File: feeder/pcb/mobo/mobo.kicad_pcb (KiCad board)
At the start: 2 copper layers, 160.6 x 110 mm, 45 parts, among them J1 SPRING_FINGER_INTERFACE, J3 SWD_10, M1 DRIVE_MOTOR, M2 PEEL_MOTOR, SW1 BUTTON_1, SW2 BUTTON_2, SW3 RESET_BUTTON, SW4 TAPE_DETECT, SW5 FILM_TENSION, U1 STM32F030K6Tx, U2 VCNT2020, U3 MAX3485, U4 DRV8833PW, U5 AP1117-33, Y1 Crystal_GND24_Small

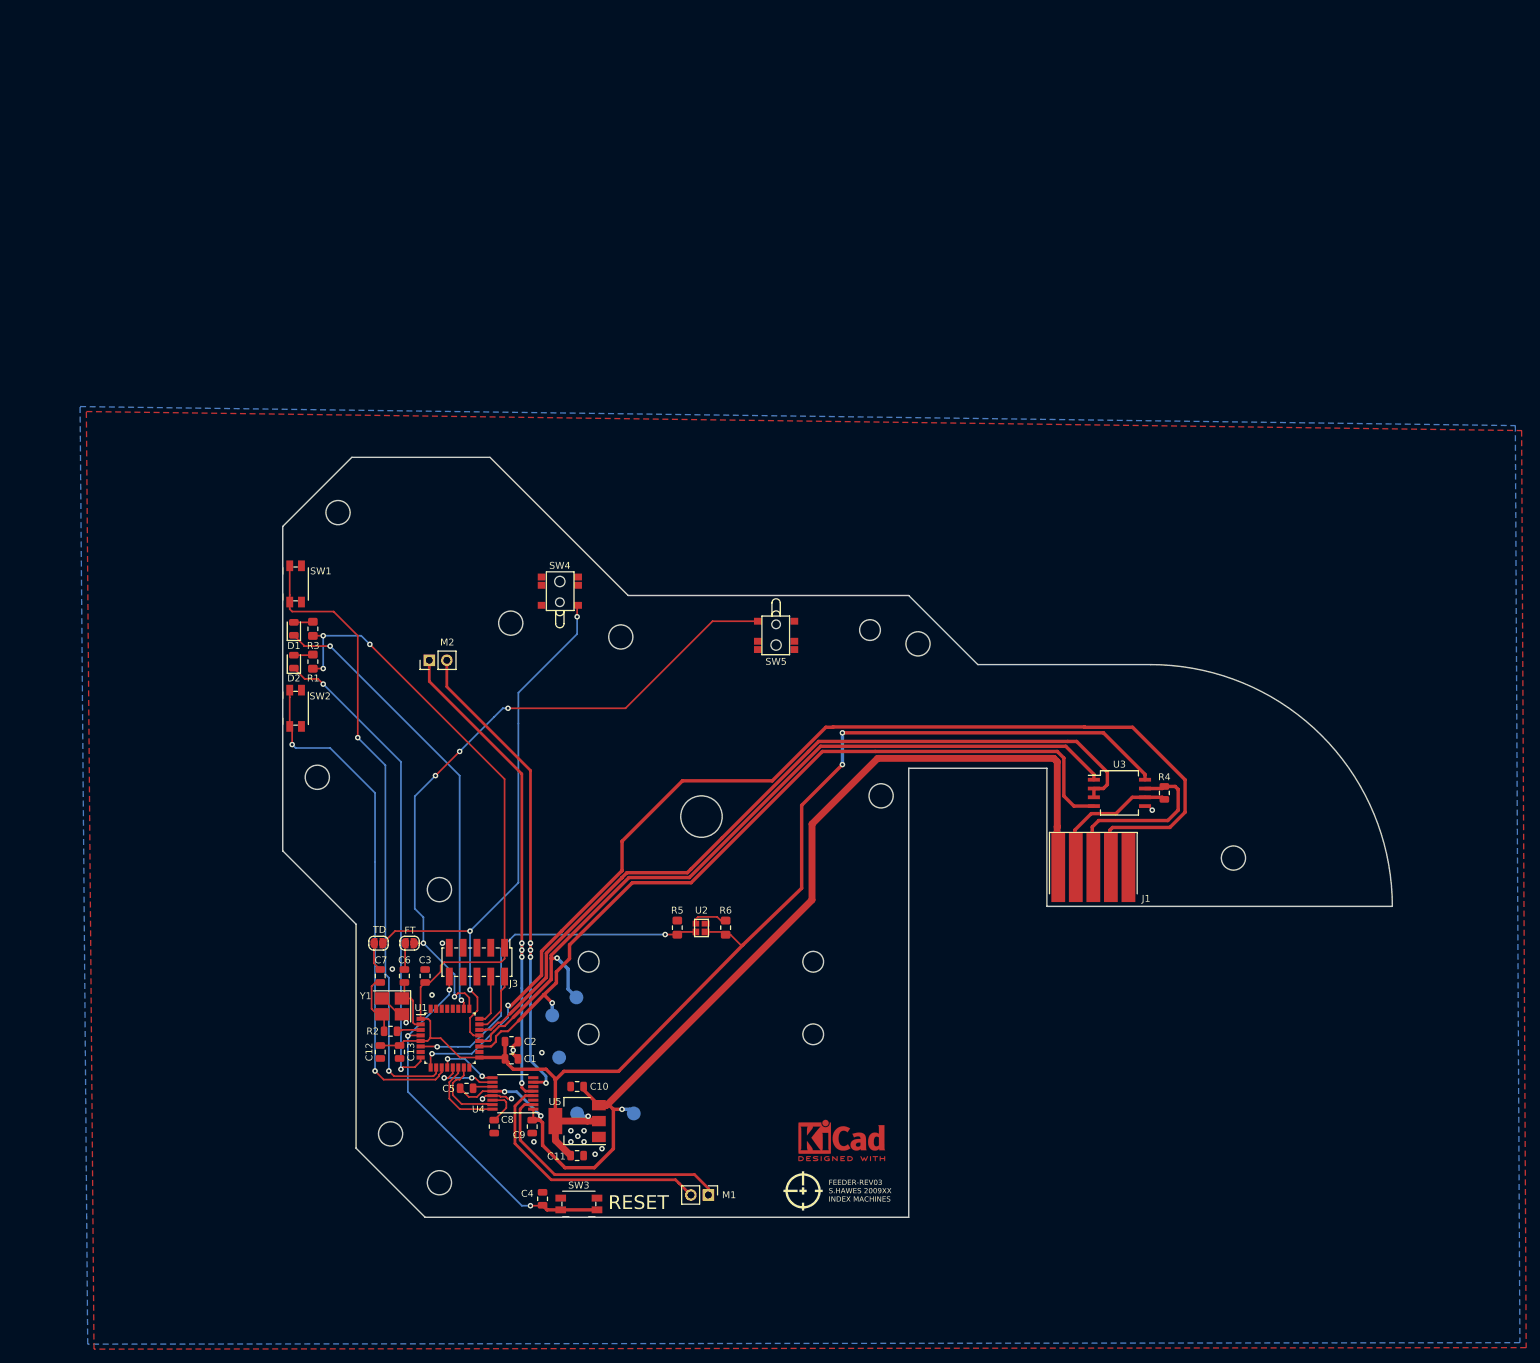
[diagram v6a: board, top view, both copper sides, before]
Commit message: this commit reflects boards ordered for rev04 of the feeder motherboard, rev02 of the indexing wheel, and rev02 of the feeder floor
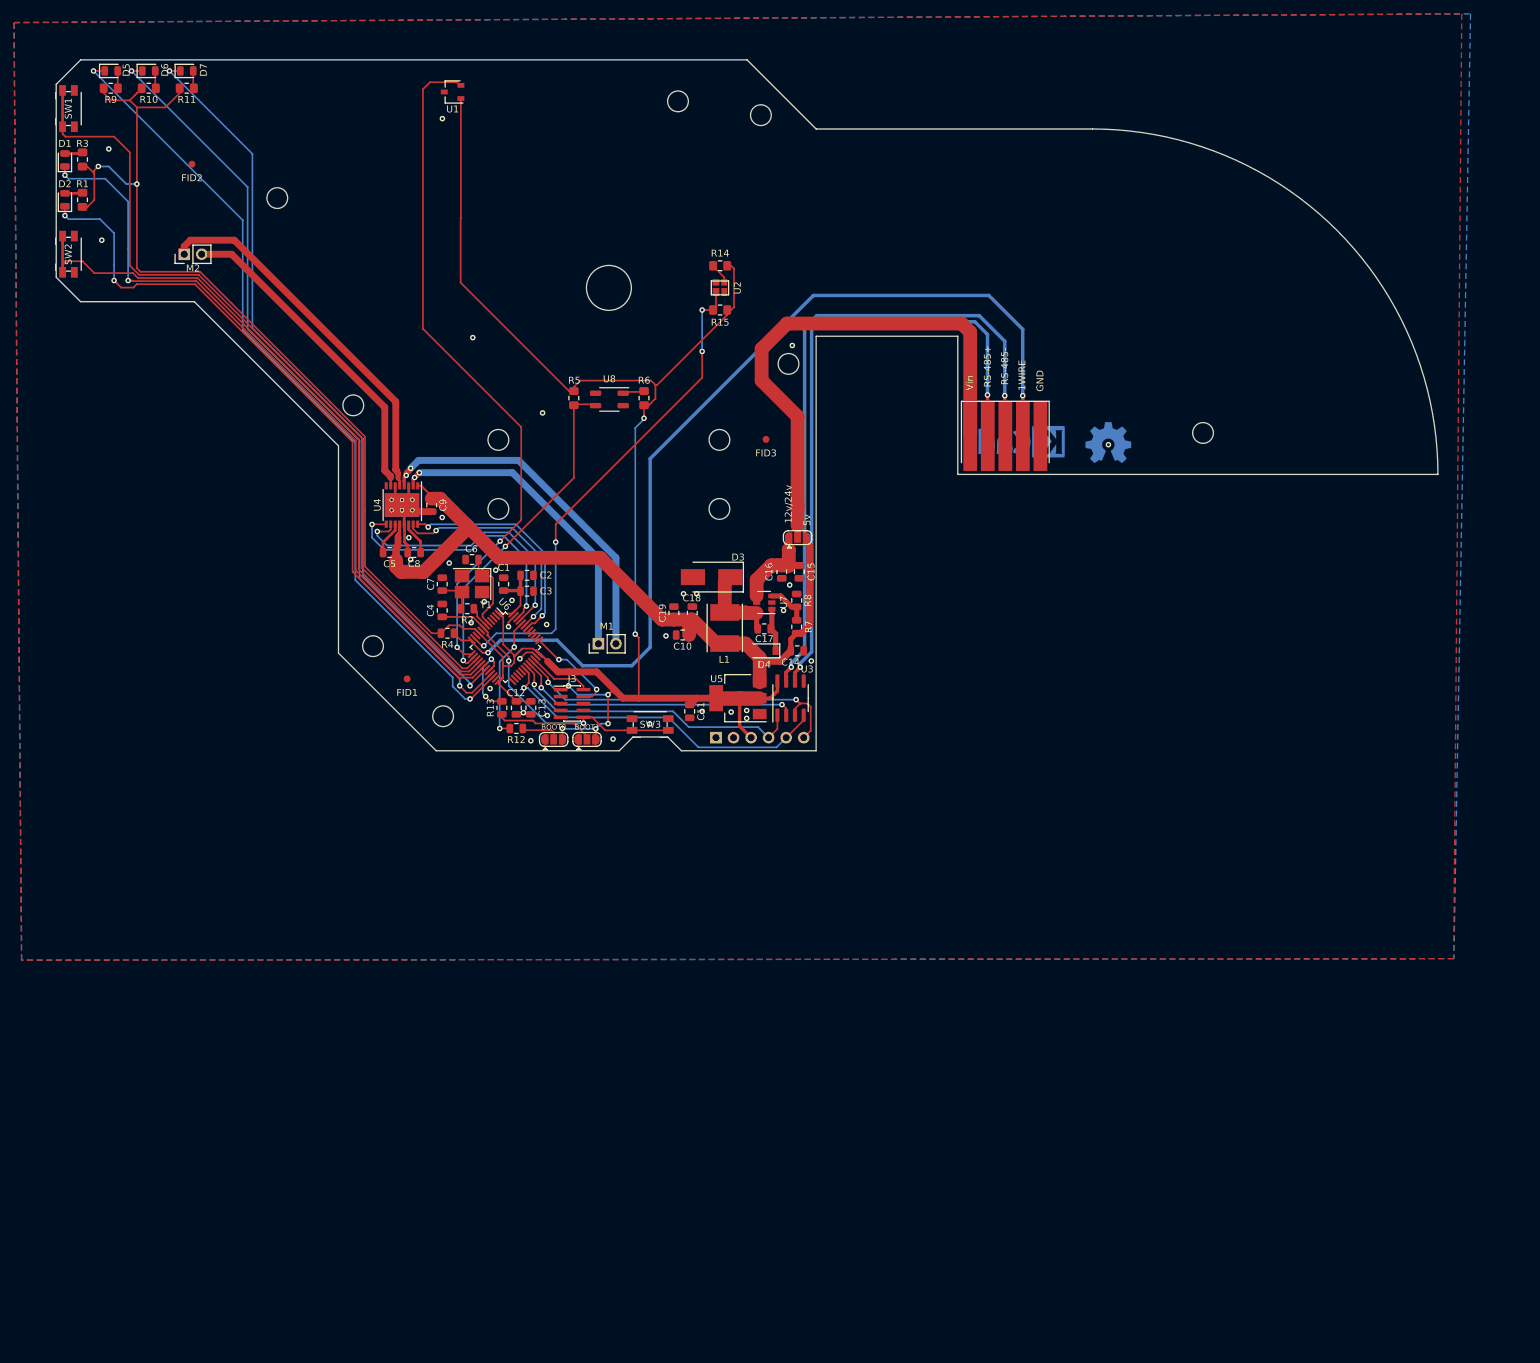
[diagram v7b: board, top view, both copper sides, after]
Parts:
- removed the REF** at (119.8, 161.8)
- removed SW4: TAPE_DETECT, index:K5-1624SA-01
- removed SW5: FILM_TENSION, index:K5-1624SA-01
- removed TP1: MCU_TX, TestPoint:TestPoint_Pad_D2.0mm
- removed TP2, TP3, TP4, TP5: MCU_RX, TestPoint:TestPoint_Pad_D2.0mm
- added C14: 100uF, Capacitor_SMD:C_0805_2012Metric, F.Cu at (113.4, 90.9)
- added C15: 4.7uF, Capacitor_SMD:C_0805_2012Metric, F.Cu at (113.7, 79.5)
- added C16: 4.7uF, Capacitor_SMD:C_0805_2012Metric, F.Cu at (111.1, 79.5)
- added C17: 0.1uF, Capacitor_SMD:C_0805_2012Metric, F.Cu at (108.6, 87.8)
- added C18: 10uF, Capacitor_SMD:C_0805_2012Metric, F.Cu at (98.2, 85.5)
- added C19: 10uF, Capacitor_SMD:C_0805_2012Metric, F.Cu at (95.5, 85.5)
- added D3: B140, Diode_SMD:D_SMB_Handsoldering, F.Cu at (101.0, 80.3)
- added D4: 1N4148, Diode_SMD:D_SOD-123, F.Cu at (108.6, 90.9)
- added D5: LED3, LED_SMD:LED_0805_2012Metric, F.Cu at (14.1, 7.00)
- added D6: LED4, LED_SMD:LED_0805_2012Metric, F.Cu at (19.5, 7.00)
- added D7: LED5, LED_SMD:LED_0805_2012Metric, F.Cu at (25.0, 7.00)
- added FID1: Fiducial, Fiducial:Fiducial_1mm_Mask2mm, F.Cu at (56.9, 95.0)
- added FID2: Fiducial, Fiducial:Fiducial_1mm_Mask2mm, F.Cu at (25.8, 20.5)
- added FID3: Fiducial, Fiducial:Fiducial_1mm_Mask2mm, F.Cu at (108.8, 60.3)
- added J2: PLATED_PADS, index:5-pad-spring-finger-interface, F.Cu at (138.4, 65.0)
- added JP3: SolderJumper_3_Open, Jumper:SolderJumper-3_P1.3mm_Open_RoundedPad1.0x1.5mm, F.Cu at (82.9, 103.8)
- added L1: 15uH, Inductor_SMD:L_Taiyo-Yuden_NR-50xx_HandSoldering, F.Cu at (102.9, 87.6)
- added R10: 470R, Resistor_SMD:R_0805_2012Metric_Pad1.15x1.40mm_HandSolder, F.Cu at (19.5, 9.50)
- added R11: 470R, Resistor_SMD:R_0805_2012Metric_Pad1.15x1.40mm_HandSolder, F.Cu at (25.0, 9.50)
- added R12: 10K, Resistor_SMD:R_0805_2012Metric, F.Cu at (72.7, 102.2)
- added R13: 10K, Resistor_SMD:R_0805_2012Metric, F.Cu at (70.6, 99.2)
- added R14: 470R, Resistor_SMD:R_0805_2012Metric_Pad1.15x1.40mm_HandSolder, F.Cu at (102.2, 35.2)
- added R15: 10K, Resistor_SMD:R_0805_2012Metric_Pad1.15x1.40mm_HandSolder, F.Cu at (102.2, 41.6)
- added R7: 52.3K, Resistor_SMD:R_0805_2012Metric, F.Cu at (113.3, 87.5)
- added R8: 10K, Resistor_SMD:R_0805_2012Metric, F.Cu at (113.3, 83.6)
- added R9: 470R, Resistor_SMD:R_0805_2012Metric_Pad1.15x1.40mm_HandSolder, F.Cu at (14.0, 9.50)
- added REF**: OSHW-Symbol_6.7x6mm_Copper, Symbol:OSHW-Symbol_6.7x6mm_Copper, B.Cu at (158.4, 60.8)
- added REF**: KiCad-Logo_5mm_Copper, Symbol:KiCad-Logo_5mm_Copper, B.Cu at (145.8, 61.0)
- added U6: STM32F103C8Tx, Package_QFP:LQFP-48_7x7mm_P0.5mm, F.Cu at (71.1, 90.4)
- added U7: MCP16301, Package_TO_SOT_SMD:SOT-23-6, F.Cu at (108.6, 83.9)
- added U8: QRE1113, OptoDevice:OnSemi_CASE100CY, F.Cu at (86.2, 54.5)
- D1: value LED1 -> LED2
- G***: moved to B.Cu
- J1: value SPRING_FINGER_INTERFACE -> FTDI_HEADER; footprint index:5-pad-spring-finger-interface -> Connector_PinHeader_2.54mm:PinHeader_1x06_P2.54mm_Vertical; moved to B.Cu
- J3: footprint Connector_PinHeader_2.00mm:PinHeader_2x05_P2.00mm_Vertical_SMD -> Connector_PinHeader_1.00mm:PinHeader_2x05_P1.00mm_Vertical_SMD
- JP1: value TAPE_DETECT_OVERRIDE -> SolderJumper_3_Open; footprint Jumper:SolderJumper-2_P1.3mm_Open_RoundedPad1.0x1.5mm -> Jumper:SolderJumper-3_P1.3mm_Open_RoundedPad1.0x1.5mm
- JP2: value FILM_TENSION -> SolderJumper_3_Open; footprint Jumper:SolderJumper-2_P1.3mm_Open_RoundedPad1.0x1.5mm -> Jumper:SolderJumper-3_P1.3mm_Open_RoundedPad1.0x1.5mm
- R2: value R_Small -> 50R
- R4: value 120R -> 1K
- SW3: value RESET_BUTTON -> RESET
- U1: value STM32F030K6Tx -> TCS40DPR; footprint Package_QFP:LQFP-32_7x7mm_P0.8mm -> Package_TO_SOT_SMD:SOT-23W
- U2: footprint stephen:VCNT2020 -> index:VCNT2020
- U3: footprint Package_SO:SO-8_5.3x6.2mm_P1.27mm -> Package_SO:SOIC-8_3.9x4.9mm_P1.27mm
- U4: value DRV8833PW -> DRV8833PWP; footprint Package_SO:TSSOP-16_4.4x5mm_P0.65mm -> Package_SO:HTSSOP-16-1EP_4.4x5mm_P0.65mm_EP3.4x5mm_Mask2.46x2.31mm_ThermalVias
- Y1: value Crystal_GND24_Small -> 8MHz
- moved G*** 138.1 mm to (199.2, 60.2), turned to 180 degrees
- moved U1 137.0 mm to (63.5, 10.0), turned to 180 degrees
- moved R4 106.3 mm to (62.7, 88.4), turned to 180 degrees
- moved U2 92.9 mm to (100.9, 39.4), turned to 0 degrees
- moved C9 91.1 mm to (60.5, 69.8)
- moved U4 86.7 mm to (56.1, 69.8), turned to 270 degrees
- moved C4 86.4 mm to (62.0, 85.1)
- moved JP1 84.4 mm to (113.4, 74.5)
- moved C8 83.9 mm to (57.9, 76.7), turned to 180 degrees
- moved M1 81.4 mm to (84.6, 89.9), turned to 90 degrees
- moved C5 78.3 mm to (54.4, 76.7), turned to 180 degrees
- moved R5 78.1 mm to (81.0, 54.4), turned to 90 degrees
- moved R6 77.5 mm to (91.2, 54.4)
- moved SW1 76.3 mm to (7.87, 12.4)
- moved R3 75.7 mm to (9.91, 19.8)
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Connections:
- D1 pad 1: LED1 -> LED2
- D2 pad 1: LED2 -> LED1
- J1 pad 1: +5V -> GND
- J1 pad 2: RS-485+ -> Net-(J1-Pad2)
- J1 pad 3: RS-485- -> +3V3
- J1 pad 4: SLOT_DETECT -> MCU_RX
- J1 pad 5: GND -> MCU_TX
- JP1 pad 1: GND -> +VDC
- JP1 pad 2: TAPE_DETECT -> +BATT
- JP2 pad 2: FILM_TENSION -> Net-(JP2-Pad2)
- R4 pad 1: RS-485+ -> 1WIRE
- R4 pad 2: RS-485- -> +3V3
- R5 pad 1: GND -> OPTO_SIG_QRE1113
- R5 pad 2: OPTO_SIG -> +3V3
- U1 pad 2: Net-(C6-Pad1) -> FILM_TENSION
- U1 pad 3: Net-(R2-Pad1) -> GND
- U2 pad 1: OPTO_SIG -> GND
- U2 pad 2: +3V3 -> OPTO_SIG_VCNT2020
- U2 pad 3: Net-(R6-Pad2) -> Net-(R14-Pad2)
- U3 pad 2: RTS -> _RE
- U3 pad 3: RTS -> DE
- U4 pad 3: Net-(U4-Pad3) -> GND
- U4 pad 6: Net-(U4-Pad6) -> GND
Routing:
- net SLOT_DETECT: track 161.8 -> 0.00 mm, vias 2 -> 0
- net 1WIRE: track 0.00 -> 142.3 mm, vias 0 -> 2
- net LED3: track 0.00 -> 120.3 mm, vias 0 -> 2
- net RTS: track 117.3 -> 0.00 mm
- net LED4: track 0.00 -> 116.4 mm, vias 0 -> 2
- net +3V3: track 268.7 -> 384.1 mm, vias 6 -> 9
- net LED5: track 0.00 -> 112.0 mm, vias 0 -> 2
- net TAPE_DETECT: track 84.0 -> 0.00 mm, vias 3 -> 0
- net +BATT: track 0.00 -> 76.7 mm
- net MCU_RX: track 119.3 -> 44.3 mm
- net RS-485+: track 20.6 -> 94.1 mm, vias 0 -> 2
- net OPTO_SIG_VCNT2020: track 0.00 -> 72.6 mm, vias 0 -> 4
- net RS-485-: track 27.5 -> 99.4 mm, vias 0 -> 2
- net MCU_TX: track 119.2 -> 49.7 mm
- net OPTO_SIG: track 52.5 -> 0.00 mm, vias 2 -> 0
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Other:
- board size 160.6 x 110 mm -> 200 x 100 mm
- net class Default: clearance 0.2 -> 0.199
- rule pad_to_mask_clearance: 0.051 -> 0.04
- rule trace_clearance: 0.2 -> 0.199
- board text added: "12v/24v"
- board text added: "1WIRE"
- board text added: "5v"
- board text added: "BOOT0"
- board text added: "BOOT1"
- board text added: "GND"
- board text added: "Index Feeder REV04"
- board text added: "RS-485+"
- board text added: "RS-485-"
- board text added: "Vin"
- board text removed: "FEEDER-REV03 S.HAWES 2009XX INDEX MACHINES"
- board text removed: "FT"
- board text removed: "RESET"
- board text removed: "TD"

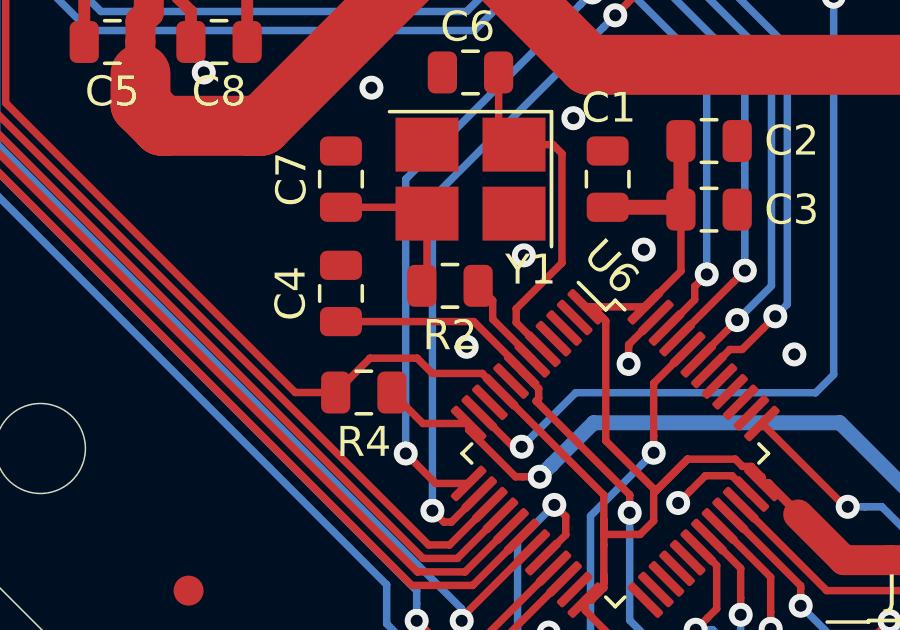
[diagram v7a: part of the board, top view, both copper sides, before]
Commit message: Updates to build the appropriate JLCPCB outputs.
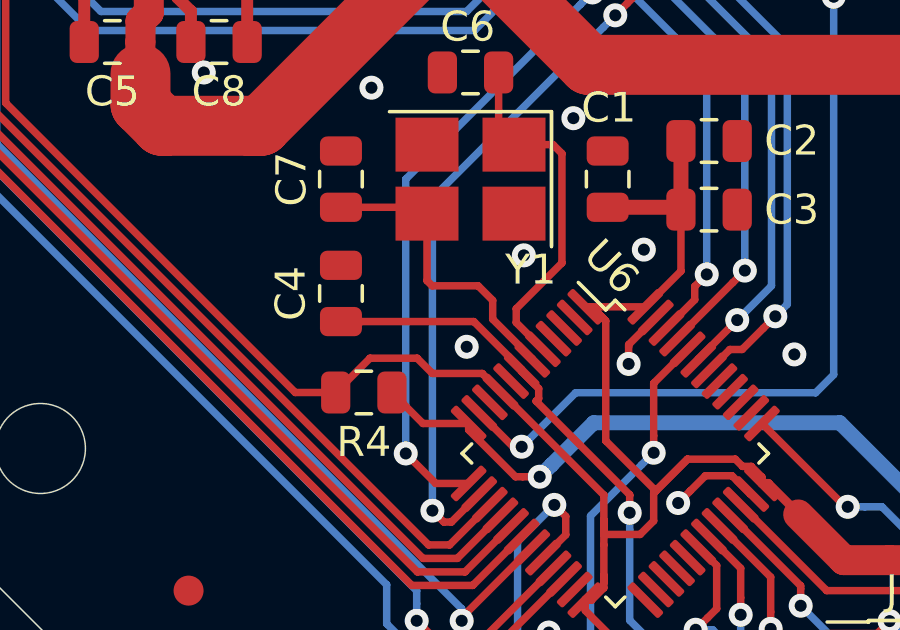
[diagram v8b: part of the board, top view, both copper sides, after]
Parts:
- removed R2: 50R, Resistor_SMD:R_0805_2012Metric
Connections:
- U6 pad 6: Net-(R2-Pad1) -> Net-(C7-Pad1)
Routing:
- net Net-(C7-Pad1): track 5.43 -> 10.2 mm
- net Net-(R2-Pad1): track 3.22 -> 0.00 mm
